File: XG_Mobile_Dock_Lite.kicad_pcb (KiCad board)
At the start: 4 copper layers, 220 x 65 mm, 57 parts, among them J1 5-1775443-8, J10 SWD, J11 UART, J12 I2C1, J13 39300240, J14 469911008, J17 8730, J2 20455-040E-76, J3 20455-040E-76, J4 3-2362375-4, J5 USB_C_Receptacle, Q16 AO3401A, Q17 2N7002W, SW1 SW_Push, U12 STM32F030C8Tx

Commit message: tweaked lite version
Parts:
- moved J17 6.43 mm to (75.6, 72.7)
- moved R63 5.40 mm to (96.7, 85.8)
- moved TP11 5.18 mm to (82.6, 77.4)
- moved J1 4.82 mm to (88.8, 80.0)
- moved J2 4.82 mm to (108.6, 80.3)
- moved J3 4.82 mm to (138.6, 80.3)
- moved TP12 4.82 mm to (82.6, 80.3)
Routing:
- net /CLKN: track 74.6 -> 69.6 mm
- net /CLKP: track 74.6 -> 69.6 mm
- net /C_RXP: track 137.7 -> 142.5 mm
- net /C_DN: track 134.8 -> 139.6 mm
- net /C_DP: track 134.3 -> 139.2 mm
- net /C_RXN: track 138.1 -> 143.0 mm
- net /HSI3P: track 32.0 -> 27.2 mm
- net /HSO6P: track 24.5 -> 19.6 mm
- net /HSO4P: track 23.6 -> 18.8 mm
- net /HSO3P: track 24.6 -> 19.8 mm
- net /HSO1P: track 25.4 -> 20.6 mm
- net /HSO0P: track 26.3 -> 21.4 mm
- net /HSO5P: track 24.0 -> 19.2 mm
- net /HSO2P: track 25.0 -> 20.2 mm
- net /HSI4P: track 31.4 -> 26.6 mm
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
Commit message: more tweaks
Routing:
- net GND: vias 50 -> 51

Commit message: more tweaks
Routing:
- net /CLKP: track 69.6 -> 66.6 mm
- net /CLKN: track 69.6 -> 66.6 mm
- net /C_TXP: track 134.0 -> 131.1 mm
- net /C_TXN: track 133.5 -> 131.1 mm
- net /HSI7P: track 30.0 -> 29.5 mm
- net /HSI7N: track 30.2 -> 29.6 mm
- net GND: vias 51 -> 146

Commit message: fixed more issues
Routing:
- net /C_TXN: track 131.1 -> 133.6 mm
- net /C_TXP: track 131.1 -> 133.7 mm
- net /CLKP: track 66.6 -> 67.3 mm
- net /CLKN: track 66.6 -> 67.3 mm

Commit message: more tweaks
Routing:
- net GND: vias 146 -> 162
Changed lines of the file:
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@@
+	)
+	(via
+		(at 99.69 61.89)
+		(size 0.4)
+		(drill 0.3)
+		(layers "F.Cu" "B.Cu")
+		(free yes)
+		(net 1)
 	)
 	(via
@@
 	)
 	(via
+		(at 103.7 61.89)
+		(size 0.4)
+		(drill 0.3)
+		(layers "F.Cu" "B.Cu")
+		(free yes)
+		(net 1)
+	)
+	(via
 		(at 115.86 73.57)
 		(size 0.4)
@@
 	)
 	(via
+		(at 127.19 61.79)
+		(size 0.4)
+		(drill 0.3)
+		(layers "F.Cu" "B.Cu")
+		(free yes)
+		(net 1)
+	)
+	(via
 		(at 134.18 86.43)
 		(size 0.4)
@@
 	(via
 		(at 102.36 73.56)
+		(size 0.4)
+		(drill 0.3)
+		(layers "F.Cu" "B.Cu")
+		(free yes)
+		(net 1)
+	)
+	(via
+		(at 109.19 61.9)
 		(size 0.4)
 		(drill 0.3)
@@
 	)
 	(via
+		(at 107.69 61.9)
+		(size 0.4)
+		(drill 0.3)
+		(layers "F.Cu" "B.Cu")
+		(free yes)
+		(net 1)
+	)
+	(via
 		(at 109.41 67.6)
 		(size 0.4)
@@
 	)
 	(via
+		(at 94.67 61.88)
+		(size 0.4)
+		(drill 0.3)
+		(layers "F.Cu" "B.Cu")
+		(free yes)
+		(net 1)
+	)
+	(via
 		(at 131.35 80.46)
 		(size 0.4)
@@
 	)
 	(via
+		(at 117.67 61.81)
+		(size 0.4)
+		(drill 0.3)
+		(layers "F.Cu" "B.Cu")
+		(free yes)
+		(net 1)
+	)
+	(via
 		(at 101.37 58.5)
 		(size 0.4)
@@
 	)
 	(via
+		(at 105.2 61.89)
+		(size 0.4)
+		(drill 0.3)
+		(layers "F.Cu" "B.Cu")
+		(free yes)
+		(net 1)
+	)
+	(via
 		(at 111.37 73.59)
 		(size 0.4)
@@
 	)
 	(via
+		(at 119.17 61.81)
+		(size 0.4)
+		(drill 0.3)
+		(layers "F.Cu" "B.Cu")
+		(free yes)
+		(net 1)
+	)
+	(via
 		(at 96.29 58.52)
 		(size 0.4)
@@
 	)
 	(via
+		(at 121.65 61.79)
+		(size 0.4)
+		(drill 0.3)
+		(layers "F.Cu" "B.Cu")
+		(free yes)
+		(net 1)
+	)
+	(via
 		(at 135.5 89)
 		(size 0.4)
@@
 	)
 	(via
+		(at 101.19 61.89)
+		(size 0.4)
+		(drill 0.3)
+		(layers "F.Cu" "B.Cu")
+		(free yes)
+		(net 1)
+	)
+	(via
 		(at 105.25 65)
 		(size 0.4)
@@
 	)
 	(via
+		(at 96.17 61.88)
+		(size 0.4)
+		(drill 0.3)
+		(layers "F.Cu" "B.Cu")
+		(free yes)
+		(net 1)
+	)
+	(via
 		(at 108.36 70.16)
 		(size 0.4)
@@
 	)
 	(via
+		(at 115.19 61.82)
+		(size 0.4)
+		(drill 0.3)
+		(layers "F.Cu" "B.Cu")
+		(free yes)
+		(net 1)
+	)
+	(via
 		(at 106.85 70.17)
 		(size 0.4)
@@
 	)
 	(via
+		(at 113.69 61.82)
+		(size 0.4)
+		(drill 0.3)
+		(layers "F.Cu" "B.Cu")
+		(free yes)
+		(net 1)
+	)
+	(via
 		(at 106.86 80.8)
 		(size 0.4)
@@
 	(via
 		(at 108.36 77.9)
+		(size 0.4)
+		(drill 0.3)
+		(layers "F.Cu" "B.Cu")
+		(free yes)
+		(net 1)
+	)
+	(via
+		(at 123.15 61.79)
 		(size 0.4)
 		(drill 0.3)
@@
 		(size 0.4)
 		(drill 0.3)
+		(layers "F.Cu" "B.Cu")
+		(free yes)
+		(net 1)
+	)
+	(via
+		(at 125.69 61.79)
+		(size 0.4)
+		(drill 0.3)

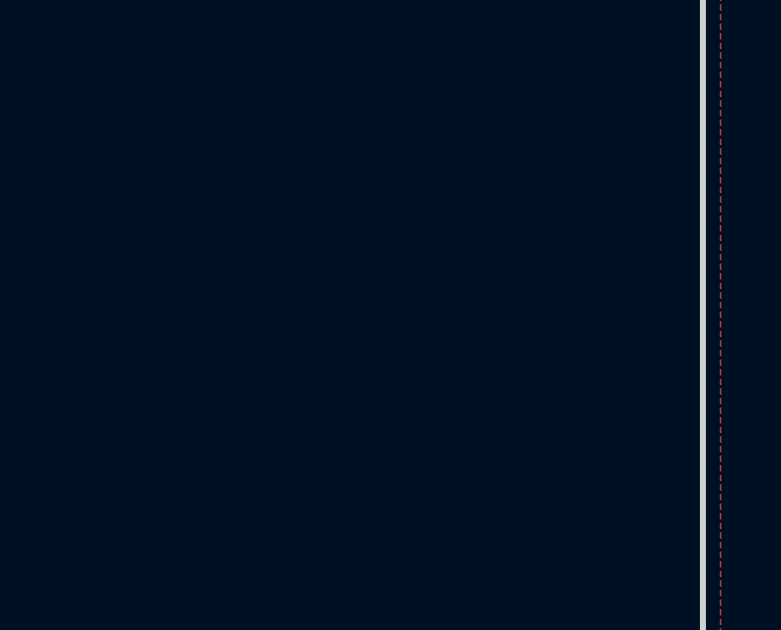
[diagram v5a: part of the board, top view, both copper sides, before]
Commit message: added extra connector for ground from the cable
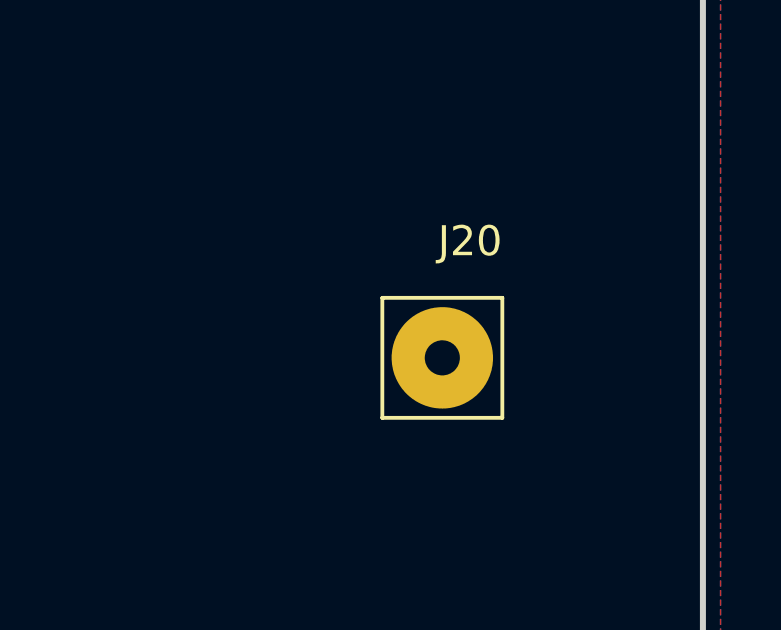
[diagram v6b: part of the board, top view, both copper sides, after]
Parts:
- added J20: 8730, KEYSTONE_8730:KEYSTONE_8730, F.Cu at (228.1, 77.7)

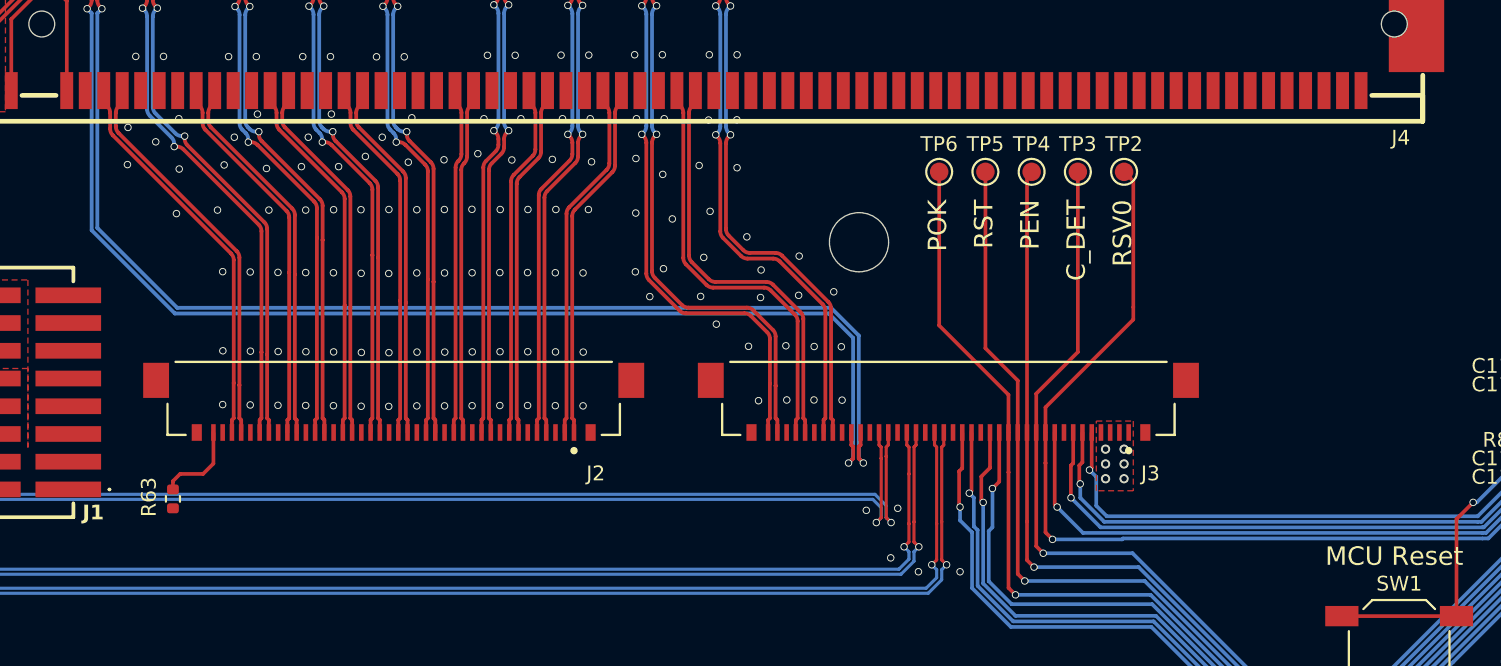
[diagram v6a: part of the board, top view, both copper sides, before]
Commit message: fixed traces
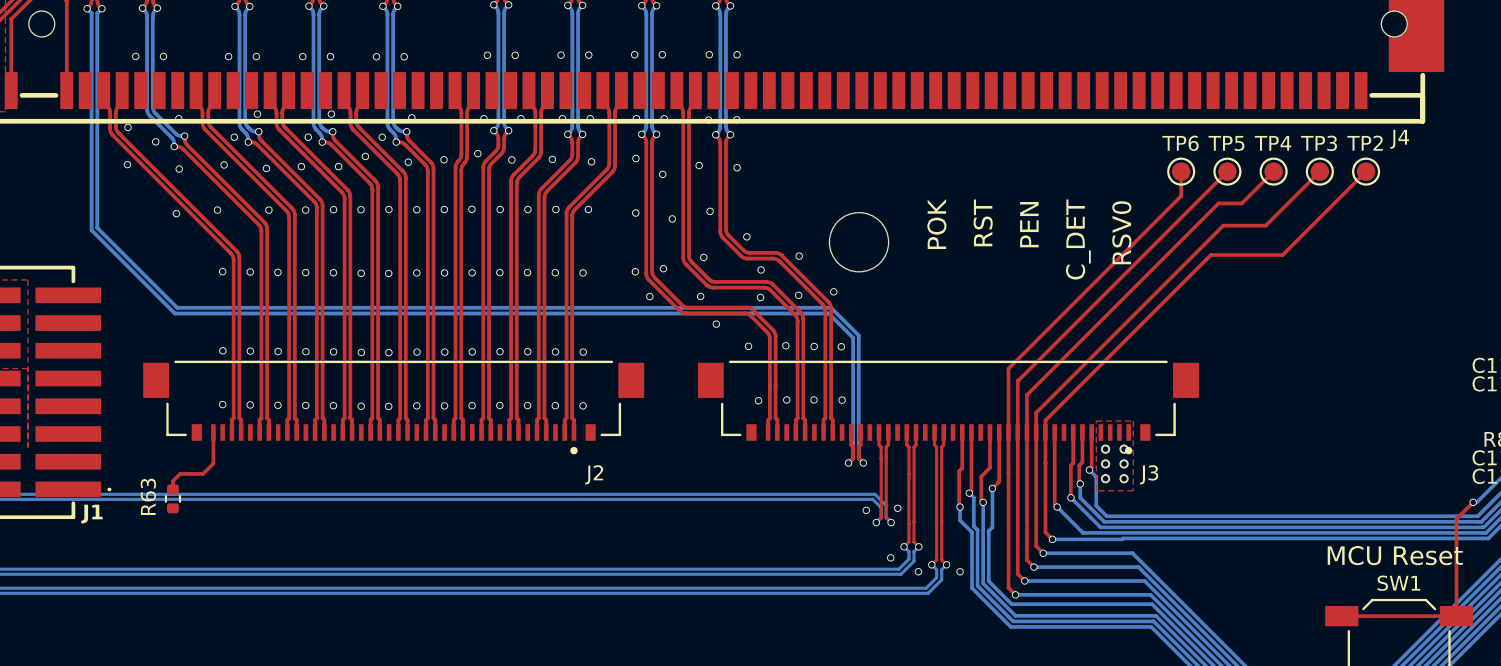
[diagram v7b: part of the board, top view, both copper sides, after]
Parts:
- moved TP2 13.1 mm to (161.2, 68.1)
- moved TP3 13.1 mm to (158.7, 68.1)
- moved TP4 13.1 mm to (156.2, 68.1)
- moved TP5 13.1 mm to (153.7, 68.1)
- moved TP6 13.1 mm to (151.2, 68.1)
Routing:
- net /RSV0: track 62.2 -> 69.5 mm
- net /CON_DET: track 62.6 -> 69.3 mm
- net /PWREN#: track 64.1 -> 70.3 mm
- net /RST#: track 67.3 -> 71.3 mm
- net /PWROK: track 64.5 -> 66.8 mm
